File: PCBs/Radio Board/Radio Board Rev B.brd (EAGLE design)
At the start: 95.9 x 90.2 mm, 4 parts

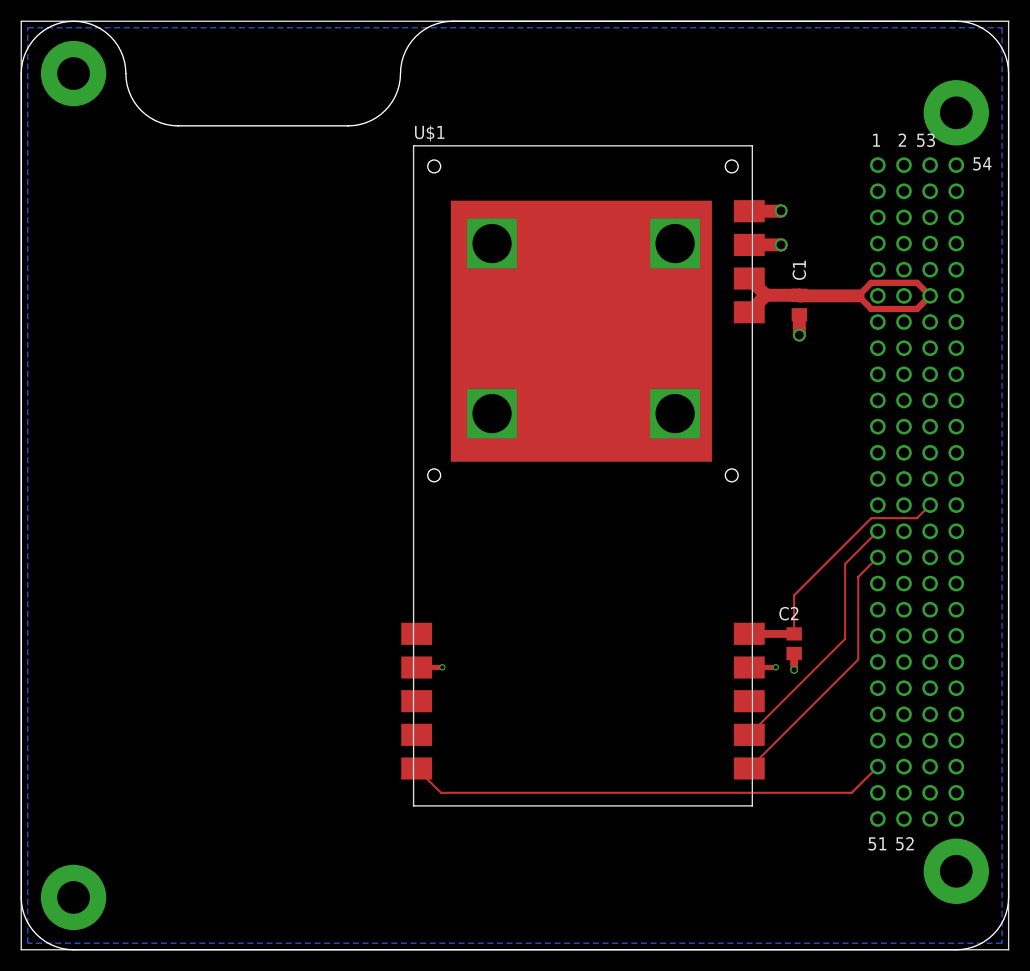
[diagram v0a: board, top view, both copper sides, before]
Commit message: Fix thermal/ground connection of radio
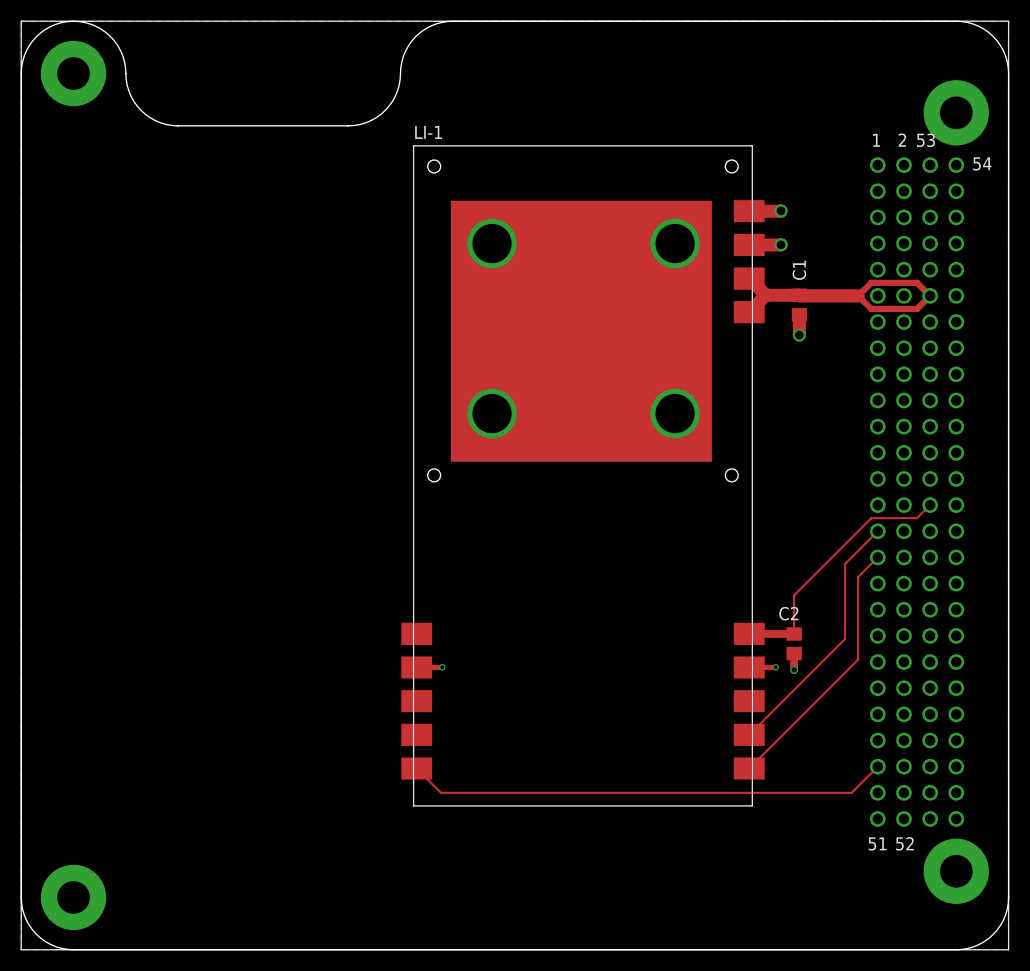
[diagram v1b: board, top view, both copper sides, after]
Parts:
- renumbered U$1 to LI-1
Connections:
- net GND: now also LI-1.THERM1, LI-1.THERM2, LI-1.THERM3, LI-1.THERM4
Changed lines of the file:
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@@
 <attribute name="VALUE" x="76.327" y="32.258" size="1.27" layer="27" rot="R270"/>
 </element>
-<element name="U$1" library="Cubesat" package="LI-1" value="LI-1" x="38.1" y="13.97"/>
+<element name="LI-1" library="Cubesat" package="LI-1" value="LI-1" x="38.1" y="13.97"/>
 <element name="U$2" library="Cubesat" package="PC104_RADIO" value="PC104_RADIO" x="0" y="0"/>
 </elements>
@@
 <signal name="GND">
 <polygon width="0.1524" layer="16">
-<vertex x="0.635" y="89.535"/>
-<vertex x="95.25" y="89.535"/>
-<vertex x="95.25" y="0.635"/>
-<vertex x="0.635" y="0.635"/>
+<vertex x="0" y="90.17"/>
+<vertex x="95.885" y="90.17"/>
+<vertex x="95.885" y="0"/>
+<vertex x="0" y="0"/>
 </polygon>
 <contactref element="C2" pad="2"/>
@@
 <wire x1="75.057" y1="28.768" x2="75.057" y2="27.178" width="0.762" layer="1"/>
 <via x="75.057" y="27.178" extent="1-16" drill="0.508"/>
-<contactref element="U$1" pad="GND1"/>
-<contactref element="U$1" pad="GND2"/>
-<contactref element="U$1" pad="RF_GND3"/>
-<contactref element="U$1" pad="RF_GND2"/>
-<contactref element="U$1" pad="RF_GND1"/>
+<contactref element="LI-1" pad="GND1"/>
+<contactref element="LI-1" pad="GND2"/>
+<contactref element="LI-1" pad="RF_GND3"/>
+<contactref element="LI-1" pad="RF_GND2"/>
+<contactref element="LI-1" pad="RF_GND1"/>
 <wire x1="75.565" y1="61.661" x2="75.565" y2="59.69" width="1.27" layer="1"/>
 <via x="75.565" y="59.69" extent="1-16" drill="0.846665625"/>
@@
 <contactref element="U$2" pad="84"/>
 <contactref element="U$2" pad="100"/>
-<wire x1="70.7" y1="68.45" x2="54.4" y2="60.07" width="0" layer="19" extent="1-1"/>
+<contactref element="LI-1" pad="THERM1"/>
+<contactref element="LI-1" pad="THERM2"/>
+<contactref element="LI-1" pad="THERM3"/>
+<contactref element="LI-1" pad="THERM4"/>
+<wire x1="45.72" y1="52.07" x2="54.4" y2="60.07" width="0" layer="19" extent="1-1"/>
 </signal>
 <signal name="SW3">
@@
 <wire x1="81.28" y1="63.5" x2="82.55" y2="64.77" width="0.6096" layer="1"/>
 <wire x1="81.28" y1="63.5" x2="82.55" y2="62.23" width="0.6096" layer="1"/>
-<contactref element="U$1" pad="V_AMP1"/>
-<contactref element="U$1" pad="V_AMP2"/>
+<contactref element="LI-1" pad="V_AMP1"/>
+<contactref element="LI-1" pad="V_AMP2"/>
 <wire x1="81.28" y1="63.5" x2="75.626" y2="63.5" width="1.27" layer="1"/>
 <wire x1="75.626" y1="63.5" x2="75.565" y2="63.561" width="1.27" layer="1"/>
@@
 </signal>
 <signal name="LITHIUM_TX">
-<contactref element="U$1" pad="TX_UART"/>
+<contactref element="LI-1" pad="TX_UART"/>
 <wire x1="81.28" y1="28.18" x2="70.7" y2="17.6" width="0.2032" layer="1"/>
 <wire x1="81.28" y1="36.195" x2="81.28" y2="28.18" width="0.2032" layer="1"/>
@@
 </signal>
 <signal name="LITHIUM_RX">
-<contactref element="U$1" pad="RX_UART"/>
+<contactref element="LI-1" pad="RX_UART"/>
 <wire x1="80.01" y1="37.465" x2="80.01" y2="30.18" width="0.2032" layer="1"/>
 <wire x1="80.01" y1="30.18" x2="70.7" y2="20.87" width="0.2032" layer="1"/>
@@
 <signal name="3V3">
 <contactref element="C2" pad="1"/>
-<contactref element="U$1" pad="3.3V"/>
+<contactref element="LI-1" pad="3.3V"/>
 <wire x1="75.057" y1="30.668" x2="70.712" y2="30.668" width="0.762" layer="1"/>
 <wire x1="70.712" y1="30.668" x2="70.7" y2="30.68" width="0.762" layer="1"/>
@@
 </signal>
 <signal name="OA_RESET">
-<contactref element="U$1" pad="CONFIG1"/>
+<contactref element="LI-1" pad="CONFIG1"/>
 <wire x1="38.4" y1="17.6" x2="40.76" y2="15.24" width="0.2032" layer="1"/>
 <wire x1="40.76" y1="15.24" x2="80.645" y2="15.24" width="0.2032" layer="1"/>

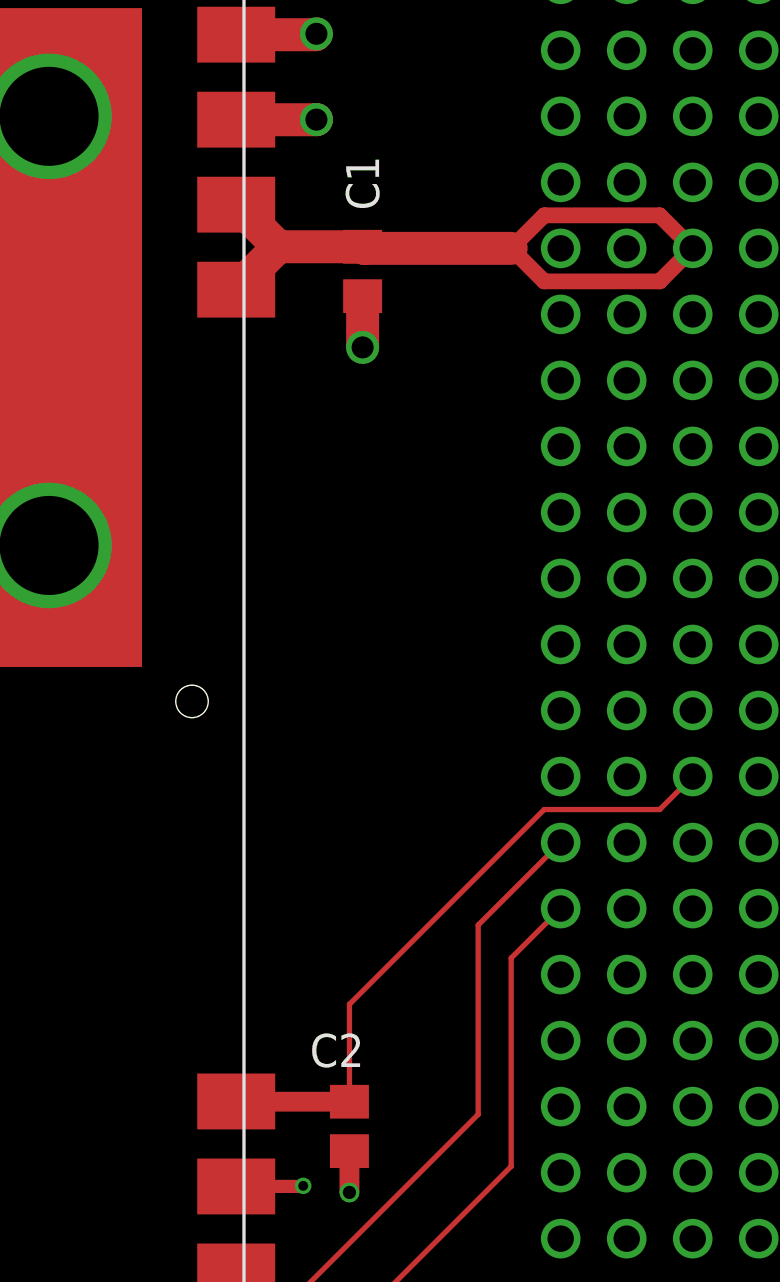
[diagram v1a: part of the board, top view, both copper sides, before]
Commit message: Update cap values
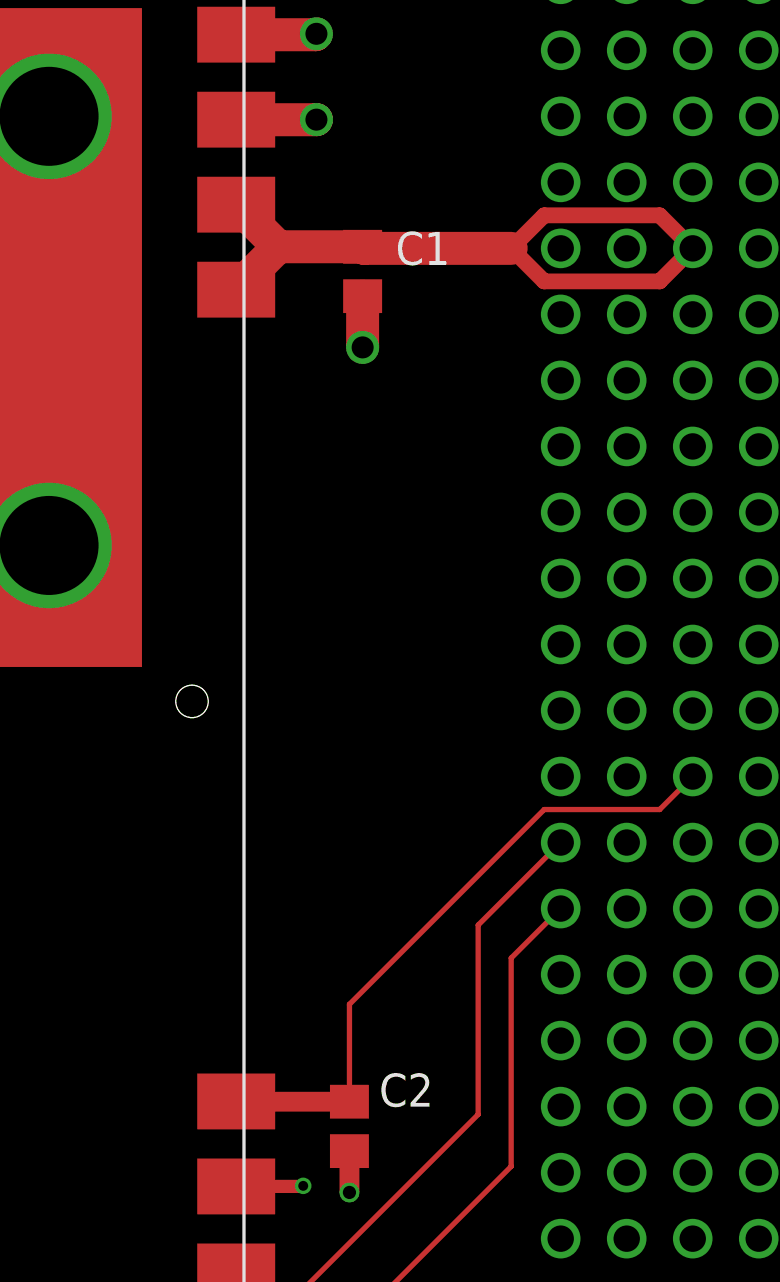
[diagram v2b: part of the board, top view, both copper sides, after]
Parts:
- C1: value 10uF -> 47uF
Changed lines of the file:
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@@
 </autorouter>
 <elements>
-<element name="C1" library="resistor" library_urn="urn:adsk.eagle:library:348" package="C0805" package3d_urn="urn:adsk.eagle:package:26137/1" value="10uF" x="75.565" y="62.611" smashed="yes" rot="R270">
-<attribute name="NAME" x="74.93" y="67.056" size="1.27" layer="25" rot="R270"/>
-<attribute name="VALUE" x="76.835" y="67.056" size="1.27" layer="27" rot="R270"/>
+<element name="C1" library="resistor" library_urn="urn:adsk.eagle:library:348" package="C0805" package3d_urn="urn:adsk.eagle:package:26137/1" value="47uF" x="75.565" y="62.611" smashed="yes" rot="R270">
+<attribute name="NAME" x="76.835" y="62.865" size="1.27" layer="25"/>
+<attribute name="VALUE" x="76.835" y="61.468" size="1.27" layer="27"/>
 </element>
 <element name="C2" library="resistor" library_urn="urn:adsk.eagle:library:348" package="C0805" package3d_urn="urn:adsk.eagle:package:26137/1" value="0.1uF" x="75.057" y="29.718" smashed="yes" rot="R270">
-<attribute name="NAME" x="73.533" y="32.004" size="1.27" layer="25"/>
-<attribute name="VALUE" x="76.327" y="32.258" size="1.27" layer="27" rot="R270"/>
+<attribute name="NAME" x="76.2" y="30.48" size="1.27" layer="25"/>
+<attribute name="VALUE" x="76.2" y="28.956" size="1.27" layer="27"/>
 </element>
 <element name="LI-1" library="Cubesat" package="LI-1" value="LI-1" x="38.1" y="13.97"/>
